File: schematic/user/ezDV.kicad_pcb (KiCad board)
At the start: 4 copper layers, 64.8 x 69.9 mm, 83 parts, among them J1 TYPE-C-31-M-04, J2 Radio_Jack, J3 User_Jack, Q1 AO3401A, Q2 AO3401A, Q3 MBT3904DW1T1, Q4 MBT3904DW1T1, Q5 MBT3904DW1T1, SW1 ESP32S3 Reset, SW2 ESP32S3 Boot Method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

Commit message: v0.4 board: more tweaks to circuit traces and new components
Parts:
- added C1: 33pF, Capacitor_SMD:C_0402_1005Metric, F.Cu at (68.0, 100.1)
- added C22: 33pF, Capacitor_SMD:C_0402_1005Metric, F.Cu at (68.6, 104.6)
- added REF**: OSHW-Symbol_6.7x6mm_SilkScreen, Symbol:OSHW-Symbol_6.7x6mm_SilkScreen, F.Cu at (96.5, 116.8)
- moved R24 5.07 mm to (86.4, 99.1), turned to -90 degrees
- moved R22 2.49 mm to (85.0, 103.7), turned to 90 degrees
- moved C16 2.46 mm to (82.6, 104.1)
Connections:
- C16 pad 1: Net-(C16-Pad1) -> TLV320_OUT_USER
- C17 pad 1: Net-(C17-Pad1) -> TLV320_OUT_RADIO
- R22 pad 1: Net-(C16-Pad1) -> User_Jack_Speaker
- R22 pad 2: TLV320_OUT_USER -> GND
- R24 pad 1: Net-(C17-Pad1) -> GND
- R24 pad 2: TLV320_OUT_RADIO -> Radio_Jack_Speaker
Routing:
- net TLV320_IN_MCLK: track 24.7 -> 14.2 mm
- net GND: track 87.4 -> 92.7 mm, vias 261 -> 262
- net TLV320_OUT_RADIO: track 7.32 -> 10.5 mm
- net User_Jack_Speaker: track 30.6 -> 33.1 mm
- net Net-(C17-Pad1): track 2.13 -> 0.00 mm
- net Radio_Jack_Speaker: track 45.3 -> 47.4 mm
- net 3.3V_PERIPH: track 41.1 -> 43.0 mm
- net TLV320_IN_RADIO: track 3.69 -> 5.28 mm
- net Net-(C16-Pad1): track 1.25 -> 0.00 mm
- net TLV320_IN_USER: track 4.22 -> 5.40 mm

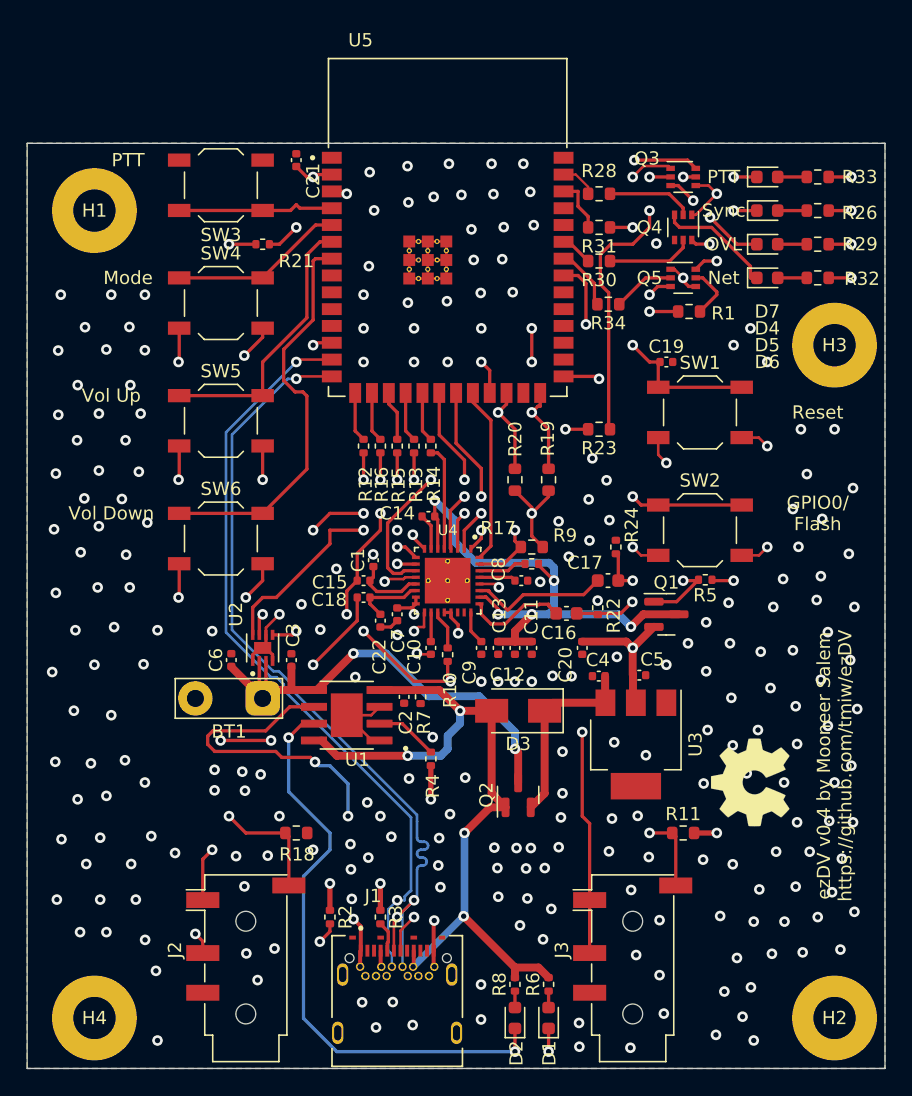
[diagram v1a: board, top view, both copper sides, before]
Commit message: v0.4 board: adjust pulldown resistors for audio I/O.
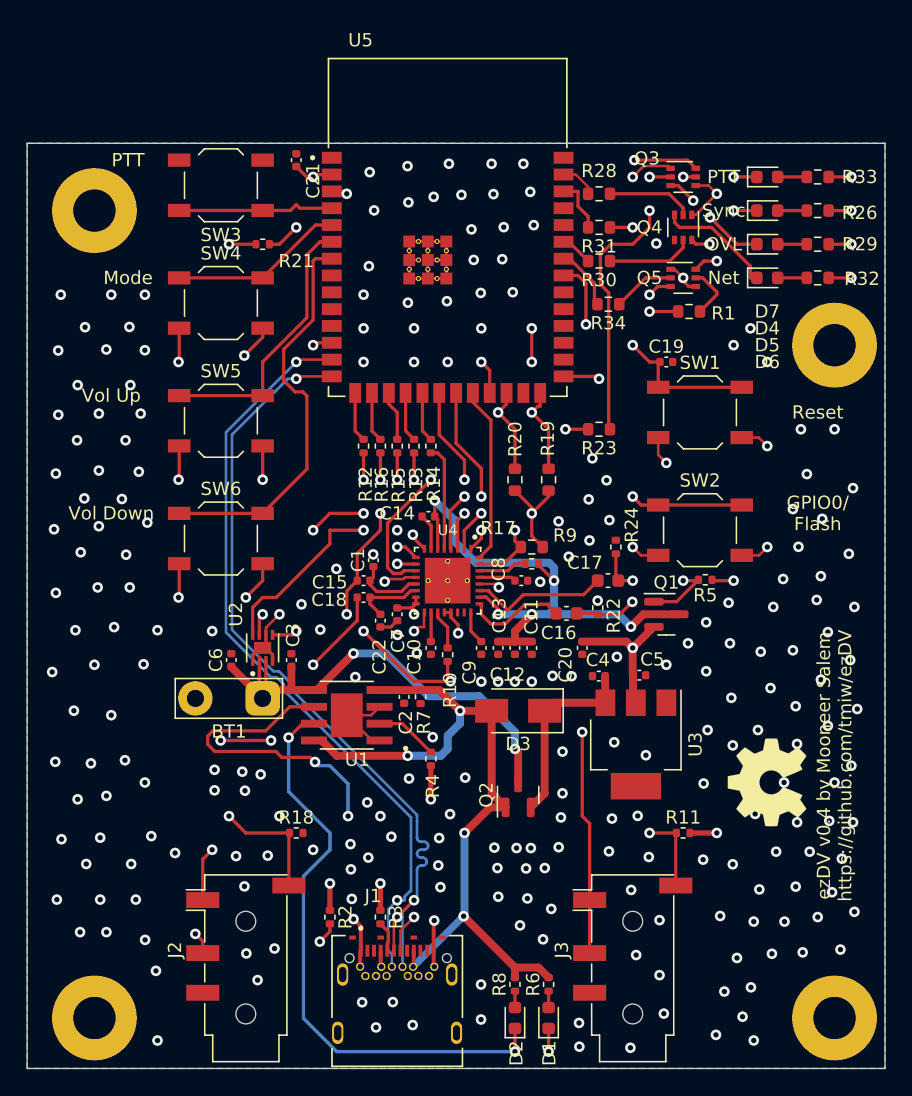
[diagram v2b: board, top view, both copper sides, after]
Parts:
- R11, R18: value 1M -> 100K; footprint Resistor_SMD:R_0603_1608Metric -> Resistor_SMD:R_0402_1005Metric
- R22, R24: value 6K -> 100K
- moved REF** 1.27 mm to (97.8, 116.8)
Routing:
- net GND: track 92.7 -> 91.7 mm

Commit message: v0.4 board: add thermistors for battery safety
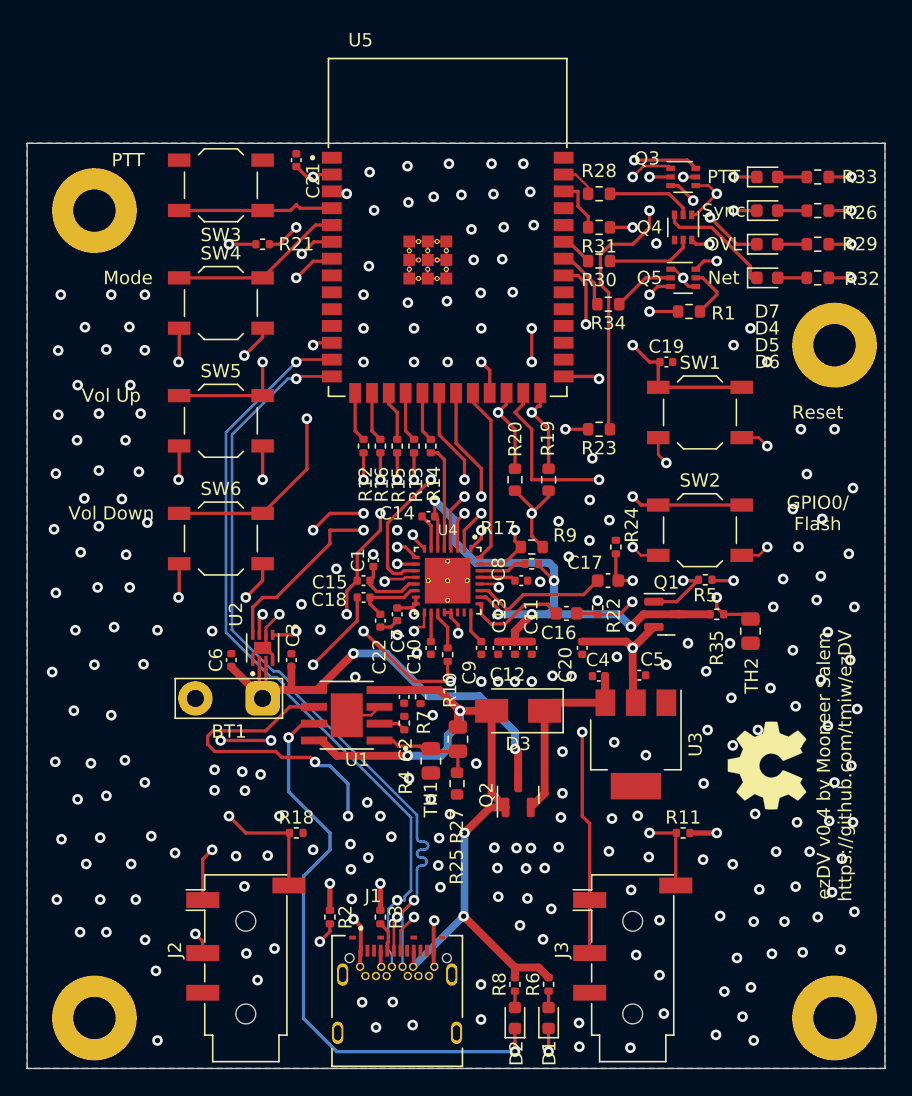
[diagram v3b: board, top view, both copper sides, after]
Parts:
- added R25: 80.6K, Resistor_SMD:R_0603_1608Metric, F.Cu at (74.4, 116.9)
- added R27: 4.87K, Resistor_SMD:R_0805_2012Metric, F.Cu at (74.4, 113.6)
- added R35: 10K, Resistor_SMD:R_0402_1005Metric, F.Cu at (94.0, 104.1)
- added TH1: SDNT2012X103F3950FTF, Resistor_SMD:R_0805_2012Metric, F.Cu at (72.4, 115.2)
- added TH2: SDNT2012X103F3950FTF, Resistor_SMD:R_0805_2012Metric, F.Cu at (96.5, 105.4)
- moved R4 3.37 mm to (70.4, 112.4), turned to 90 degrees
- moved REF** 1.27 mm to (97.8, 115.6)
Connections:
- U1 pad 1: GND -> TP4056_NTC
- U5 pad 25: unconnected-(U5-Pad25) -> GPIO25_BOARD_TEMP
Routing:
- net GPIO25_BOARD_TEMP: track 0.00 -> 30.0 mm, vias 0 -> 2
- net TP4056_NTC: track 0.00 -> 7.48 mm
- net GND: track 91.7 -> 85.9 mm, vias 262 -> 258
- net Net-(R4-Pad1): track 4.77 -> 2.06 mm
- net 3.3V_PERIPH: track 43.0 -> 45.4 mm
- net USBC_VBUS: track 61.8 -> 63.1 mm
- net GPIO6_VOL_UP: track 20.6 -> 20.9 mm, vias 0 -> 2
- net GPIO7_VOL_DOWN: track 30.2 -> 30.1 mm, vias 0 -> 2

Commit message: v0.4 board submitted for build/assembly.
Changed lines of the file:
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@@
   )
   (paper "A4")
+  (title_block
+    (title "ezDV")
+    (date "2022-10-01")
+    (rev "v0.4")
+    (company "FreeDV Project")
+  )
   (layers
     (0 "F.Cu" signal)
@@
     (fp_line (start -1 0.625) (end -1 -0.625) (layer "F.Fab") (width 0.1))
     (fp_line (start -1 -0.625) (end 1 -0.625) (layer "F.Fab") (width 0.1))
-    (pad "1" smd roundrect (at -0.9125 0 90) (size 1.025 1.4) (layers "F.Cu" "F.Paste" "F.Mask") (roundrect_rratio 0.243902)
+    (pad "1" smd roundrect (at -0.9125 0 90) (size 1.025 1.4) (layers "F.Cu" "F.Paste" "F.Mask") (roundrect_rratio 0.243902439)
       (net 2 "GND") (pintype "passive"))
-    (pad "2" smd roundrect (at 0.9125 0 90) (size 1.025 1.4) (layers "F.Cu" "F.Paste" "F.Mask") (roundrect_rratio 0.243902)
+    (pad "2" smd roundrect (at 0.9125 0 90) (size 1.025 1.4) (layers "F.Cu" "F.Paste" "F.Mask") (roundrect_rratio 0.243902439)
       (net 96 "TP4056_NTC") (pintype "passive"))
     (model "${KICAD6_3DMODEL_DIR}/Resistor_SMD.3dshapes/R_0805_2012Metric.wrl"
@@
     )
   )
-  (footprint "Capacitor_SMD:C_0402_1005Metric" (layer "F.Cu")
+  (footprint "Capacitor_SMD:C_0402_1005Metric" locked (layer "F.Cu")
     (at 72.39 106.68 90)
     (descr "Capacitor SMD 0402 (1005 Metric), square (rectangular) end terminal, IPC_7351 nominal, (Body size source: IPC-SM-782 page 76, https://www.pcb-3d.com/wordpress/wp-content/uploads/ipc-sm-782a_amendment_1_and_2.pdf), generated with kicad-footprint-generator")
@@
     (fp_line (start -0.5 -0.25) (end 0.5 -0.25) (layer "F.Fab") (width 0.1))
     (fp_line (start 0.5 0.25) (end -0.5 0.25) (layer "F.Fab") (width 0.1))
-    (pad "1" smd roundrect (at -0.48 0 90) (size 0.56 0.62) (layers "F.Cu" "F.Paste" "F.Mask") (roundrect_rratio 0.25)
+    (pad "1" smd roundrect locked (at -0.48 0 90) (size 0.56 0.62) (layers "F.Cu" "F.Paste" "F.Mask") (roundrect_rratio 0.25)
       (net 2 "GND") (pintype "passive"))
-    (pad "2" smd roundrect (at 0.48 0 90) (size 0.56 0.62) (layers "F.Cu" "F.Paste" "F.Mask") (roundrect_rratio 0.25)
+    (pad "2" smd roundrect locked (at 0.48 0 90) (size 0.56 0.62) (layers "F.Cu" "F.Paste" "F.Mask") (roundrect_rratio 0.25)
       (net 9 "TLV320_REF") (pintype "passive"))
     (model "${KICAD6_3DMODEL_DIR}/Capacitor_SMD.3dshapes/C_0402_1005Metric.wrl"
@@
     (fp_line (start 1 -0.625) (end 1 0.625) (layer "F.Fab") (width 0.1))
     (fp_line (start -1 -0.625) (end 1 -0.625) (layer "F.Fab") (width 0.1))
-    (pad "1" smd roundrect (at -0.9125 0 270) (size 1.025 1.4) (layers "F.Cu" "F.Paste" "F.Mask") (roundrect_rratio 0.243902)
+    (pad "1" smd roundrect (at -0.9125 0 270) (size 1.025 1.4) (layers "F.Cu" "F.Paste" "F.Mask") (roundrect_rratio 0.243902439)
       (net 3 "USBC_VBUS") (pintype "passive"))
-    (pad "2" smd roundrect (at 0.9125 0 270) (size 1.025 1.4) (layers "F.Cu" "F.Paste" "F.Mask") (roundrect_rratio 0.243902)
+    (pad "2" smd roundrect (at 0.9125 0 270) (size 1.025 1.4) (layers "F.Cu" "F.Paste" "F.Mask") (roundrect_rratio 0.243902439)
       (net 96 "TP4056_NTC") (pintype "passive"))
     (model "${KICAD6_3DMODEL_DIR}/Resistor_SMD.3dshapes/R_0805_2012Metric.wrl"
@@
     (fp_line (start 1 -0.625) (end 1 0.625) (layer "F.Fab") (width 0.1))
     (fp_line (start 1 0.625) (end -1 0.625) (layer "F.Fab") (width 0.1))
-    (pad "1" smd roundrect (at -0.9125 0 270) (size 1.025 1.4) (layers "F.Cu" "F.Paste" "F.Mask") (roundrect_rratio 0.243902)
+    (pad "1" smd roundrect (at -0.9125 0 270) (size 1.025 1.4) (layers "F.Cu" "F.Paste" "F.Mask") (roundrect_rratio 0.243902439)
       (net 97 "GPIO25_BOARD_TEMP") (pintype "passive"))
-    (pad "2" smd roundrect (at 0.9125 0 270) (size 1.025 1.4) (layers "F.Cu" "F.Paste" "F.Mask") (roundrect_rratio 0.243902)
+    (pad "2" smd roundrect (at 0.9125 0 270) (size 1.025 1.4) (layers "F.Cu" "F.Paste" "F.Mask") (roundrect_rratio 0.243902439)
       (net 2 "GND") (pintype "passive"))
     (model "${KICAD6_3DMODEL_DIR}/Resistor_SMD.3dshapes/R_0805_2012Metric.wrl"

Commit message: v0.5 board: reroute headset detect trace to avoid noise pickup.
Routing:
- net TLV320_IN_DETECT: track 55.3 -> 58.4 mm, vias 6 -> 5
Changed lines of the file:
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@@
   (segment (start 72.41 106.18) (end 72.39 106.2) (width 0.25) (layer "F.Cu") (net 9))
   (segment (start 72.41 104) (end 72.41 106.18) (width 0.25) (layer "F.Cu") (net 9))
-  (segment (start 68.58 97.79) (end 68.58 96.52) (width 0.25) (layer "F.Cu") (net 10))
   (segment (start 90.93 120.65) (end 90.88 120.7) (width 0.25) (layer "F.Cu") (net 10))
   (segment (start 71.031057 98.129796) (end 71.031057 98.321057) (width 0.25) (layer "F.Cu") (net 10))
   (segment (start 73.874628 109.198638) (end 71.098638 109.198638) (width 0.25) (layer "F.Cu") (net 10))
   (segment (start 71.031057 98.321057) (end 71.91 99.2) (width 0.25) (layer "F.Cu") (net 10))
-  (segment (start 66.83 101.6) (end 66.83 99.54) (width 0.25) (layer "F.Cu") (net 10))
   (segment (start 71.098638 109.198638) (end 67.31 105.41) (width 0.25) (layer "F.Cu") (net 10))
   (segment (start 73.66 107.95) (end 73.66 108.98401) (width 0.25) (layer "F.Cu") (net 10))
@@
   (segment (start 66.04 102.39) (end 66.04 104.14) (width 0.25) (layer "F.Cu") (net 10))
   (segment (start 66.83 101.6) (end 66.04 102.39) (width 0.25) (layer "F.Cu") (net 10))
-  (segment (start 66.83 99.54) (end 68.58 97.79) (width 0.25) (layer "F.Cu") (net 10))
   (via (at 67.31 105.41) (size 0.8) (drill 0.4) (layers "F.Cu" "B.Cu") (net 10))
-  (via (at 68.58 96.52) (size 0.8) (drill 0.4) (layers "F.Cu" "B.Cu") (free) (net 10))
   (via (at 73.874628 109.198638) (size 0.8) (drill 0.4) (layers "F.Cu" "B.Cu") (free) (net 10))
   (via (at 71.031057 98.129796) (size 0.8) (drill 0.4) (layers "F.Cu" "B.Cu") (free) (net 10))
   (via (at 88.9 120.65) (size 0.8) (drill 0.4) (layers "F.Cu" "B.Cu") (free) (net 10))
   (via (at 66.04 104.14) (size 0.8) (drill 0.4) (layers "F.Cu" "B.Cu") (free) (net 10))
-  (segment (start 71.031057 97.703849) (end 70.297208 96.97) (width 0.25) (layer "In2.Cu") (net 10))
-  (segment (start 70.297208 96.97) (end 69.03 96.97) (width 0.25) (layer "In2.Cu") (net 10))
   (segment (start 73.66 109.413266) (end 73.66 116.84) (width 0.25) (layer "In2.Cu") (net 10))
   (segment (start 66.04 104.14) (end 67.31 105.41) (width 0.25) (layer "In2.Cu") (net 10))
@@
   (segment (start 77.47 120.65) (end 73.66 116.84) (width 0.25) (layer "In2.Cu") (net 10))
   (segment (start 73.874628 109.198638) (end 73.66 109.413266) (width 0.25) (layer "In2.Cu") (net 10))
-  (segment (start 71.031057 98.129796) (end 71.031057 97.703849) (width 0.25) (layer "In2.Cu") (net 10))
-  (segment (start 69.03 96.97) (end 68.58 96.52) (width 0.25) (layer "In2.Cu") (net 10))
+  (segment (start 73.727614 109.051624) (end 73.874628 109.198638) (width 0.25) (layer "B.Cu") (net 10))
+  (segment (start 73.727614 104.207614) (end 73.727614 109.051624) (width 0.25) (layer "B.Cu") (net 10))
+  (segment (start 72.71 99.808739) (end 72.71 103.19) (width 0.25) (layer "B.Cu") (net 10))
+  (segment (start 72.71 103.19) (end 73.727614 104.207614) (width 0.25) (layer "B.Cu") (net 10))
+  (segment (start 71.031057 98.129796) (end 72.71 99.808739) (width 0.25) (layer "B.Cu") (net 10))
   (segment (start 68.049508 101.340492) (end 67.79 101.6) (width 0.25) (layer "F.Cu") (net 11))
   (segment (start 70.743378 101.85) (end 71.26 101.85) (width 0.25) (layer "F.Cu") (net 11))

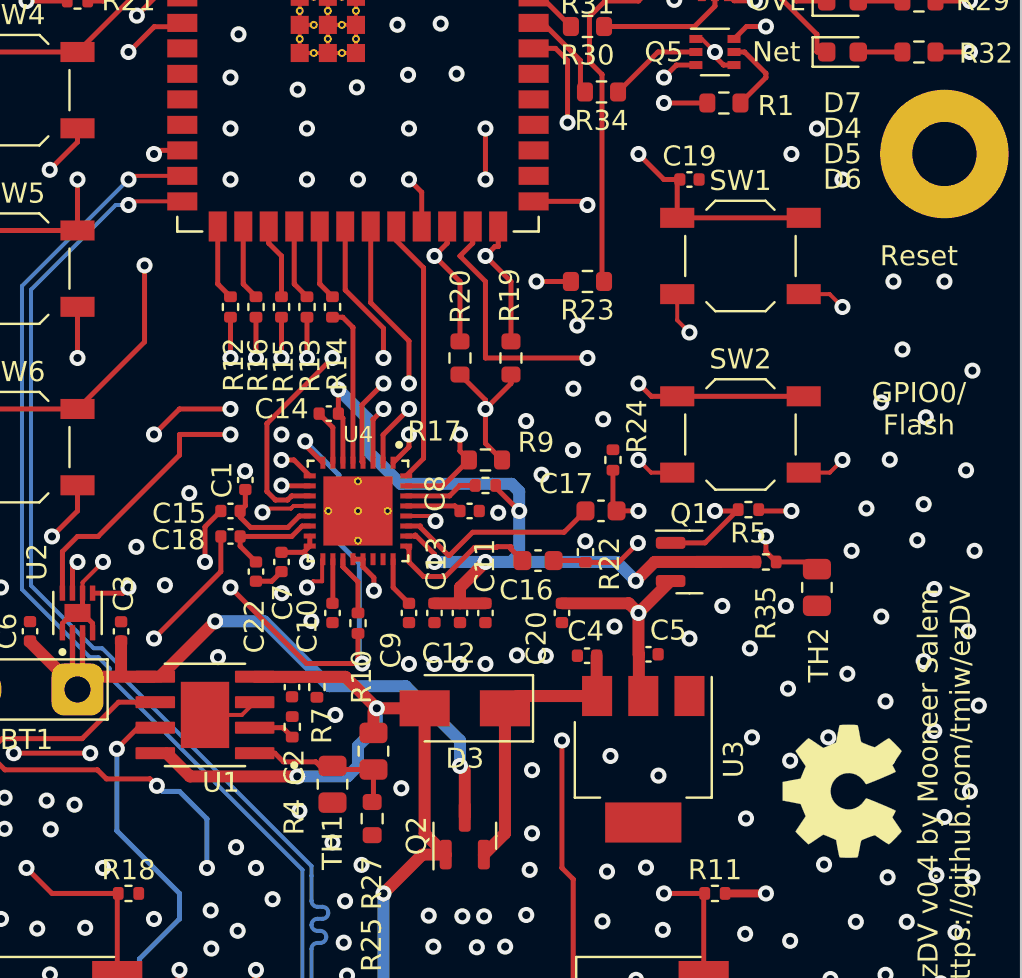
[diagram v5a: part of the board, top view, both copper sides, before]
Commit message: v0.5 board: reroute temp sensor ADC to GPIO 18.
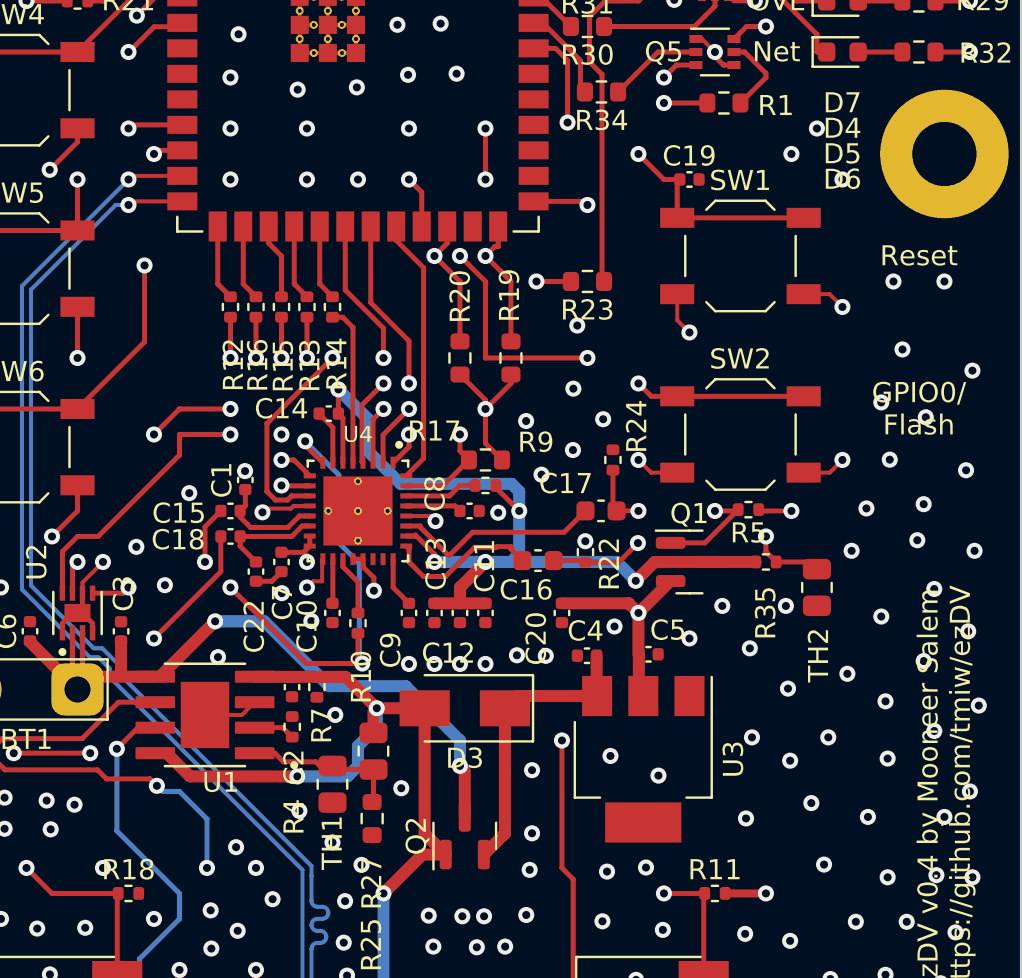
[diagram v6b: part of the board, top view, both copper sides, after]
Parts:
- removed REF**: OSHW-Symbol_6.7x6mm_SilkScreen, Symbol:OSHW-Symbol_6.7x6mm_SilkScreen
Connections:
- J1 pad S1: (no net) -> unconnected-(J1-PadS1)
- J1 pad S2: (no net) -> unconnected-(J1-PadS1)
- J1 pad S3: (no net) -> unconnected-(J1-PadS1)
- J1 pad S4: (no net) -> unconnected-(J1-PadS1)
- J1 pad S5: (no net) -> unconnected-(J1-PadS1)
- J1 pad S6: (no net) -> unconnected-(J1-PadS1)
- J1 pad S7: (no net) -> unconnected-(J1-PadS1)
- J1 pad S8: (no net) -> unconnected-(J1-PadS1)
- R35 pad 2: GPIO25_BOARD_TEMP -> GPIO18_BOARD_TEMP
- TH2 pad 1: GPIO25_BOARD_TEMP -> GPIO18_BOARD_TEMP
- U4 pad 34: GND -> (no net)
- U4 pad 35: GND -> (no net)
- U4 pad 36: GND -> (no net)
- U4 pad 37: GND -> (no net)
- U4 pad 38: GND -> (no net)
- U5 pad 11: unconnected-(U5-Pad11) -> GPIO18_BOARD_TEMP
- U5 pad 25: GPIO25_BOARD_TEMP -> unconnected-(U5-Pad25)
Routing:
- net GPIO18_BOARD_TEMP: track 0.00 -> 50.8 mm, vias 0 -> 4
- net GPIO25_BOARD_TEMP: track 30.0 -> 0.00 mm, vias 2 -> 0
